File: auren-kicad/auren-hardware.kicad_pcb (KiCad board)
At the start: 2 copper layers, 24 x 18 mm, 11 parts, among them J1 USB_B_Mini, J2 USB_B_Mini, J3 Speaker_1, J4 Speaker_2, J5 Speaker_1, J6 Speaker_2

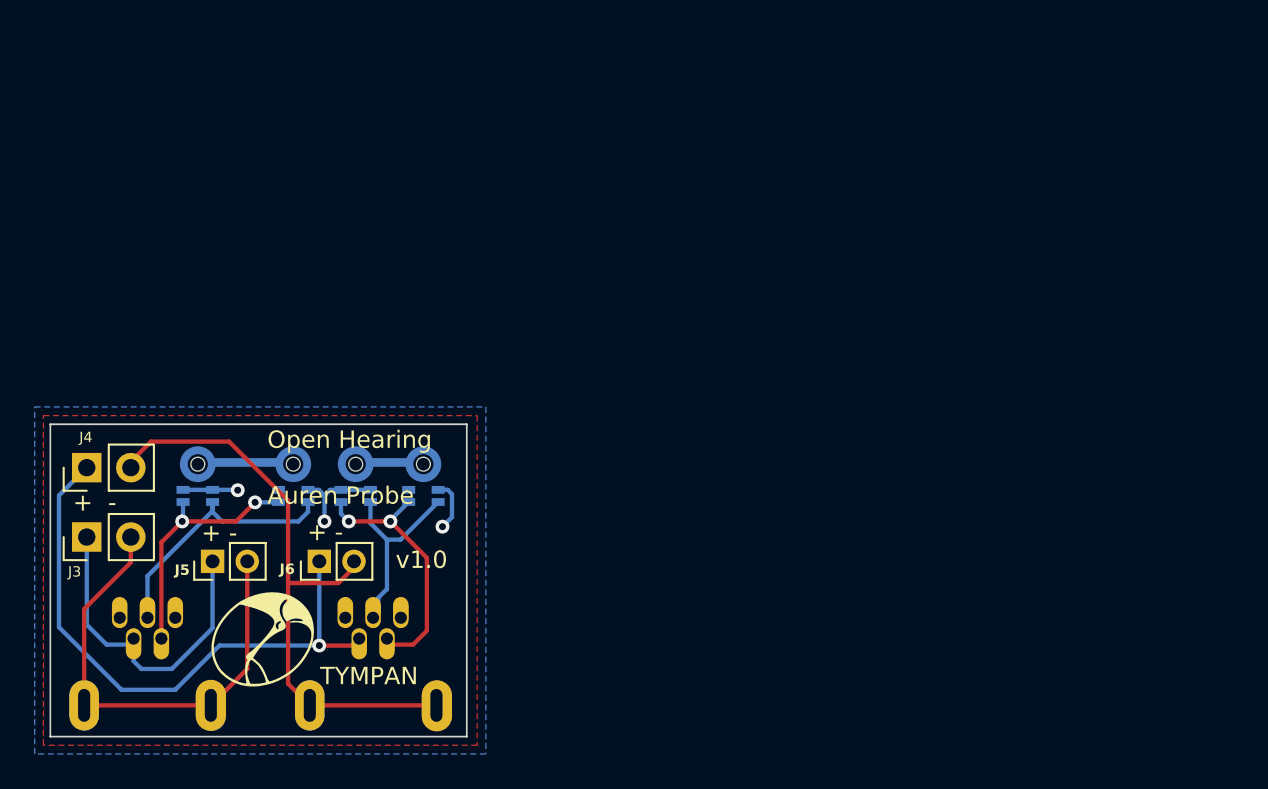
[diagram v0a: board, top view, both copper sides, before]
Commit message: Added outline shape files
Imported DXF to PCB layout file and converted to board outline.
Rough component placement
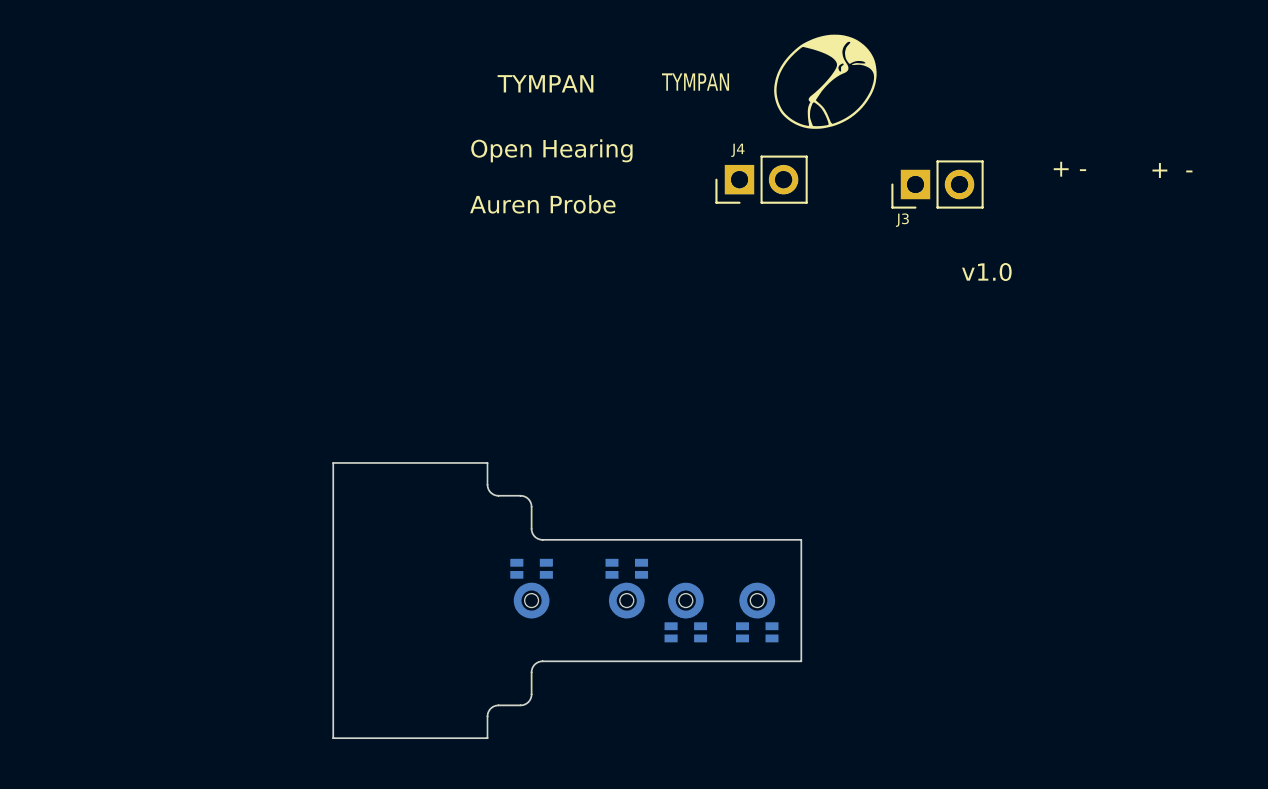
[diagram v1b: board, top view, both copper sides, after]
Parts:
- removed J1, J2: USB_B_Mini, Flywheel:MOLEX_56579-0519
- removed J5: Speaker_1, Connector_PinHeader_2.00mm:PinHeader_1x02_P2.00mm_Vertical
- removed J6: Speaker_2, Connector_PinHeader_2.00mm:PinHeader_1x02_P2.00mm_Vertical
- moved J3 51.9 mm to (169.4, 81.2)
- moved G*** 45.7 mm to (164.2, 75.3)
- moved J4 41.1 mm to (159.2, 80.9)
- moved MIC4 20.8 mm to (160.2, 105.2)
- moved MIC1 20.8 mm to (147.2, 105.2), turned to -90 degrees
- moved MIC2 20.8 mm to (152.7, 105.2), turned to -90 degrees
- moved MIC3 20.6 mm to (156.1, 105.2)
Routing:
- net /SPK2-: track 35.4 -> 0.00 mm
- net /SPK2+: track 34.7 -> 0.00 mm, vias 1 -> 0
- net /SPK1-: track 27.9 -> 0.00 mm
- net /SPK1+: track 19.2 -> 0.00 mm
- net /DAT_1: track 15.3 -> 0.00 mm
- net /CLK_2: track 15.2 -> 0.00 mm, vias 2 -> 0
- net /CLK_1: track 14.4 -> 0.00 mm, vias 2 -> 0
- net VDD: track 11.5 -> 0.00 mm, vias 3 -> 0
- net /DAT_2: track 11.2 -> 0.00 mm
- net GND: track 10.6 -> 0.00 mm
- removed copper zone on B.Cu, net GND
- removed copper zone on F.Cu, net VDD
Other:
- board size 24 x 18 mm -> 27 x 15.9 mm
- board text added: "1"
- board text added: "2"
- board text added: "3"
- board text added: "4"
- board text added: "A"
- board text added: "B"
- board text added: "C"
- board text added: "D"
- board text added: "MIC ports are 0.8mm diameter"

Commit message: minor edit
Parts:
- moved J3 32.3 mm to (142.5, 99.1), turned to 0 degrees
- moved J4 28.2 mm to (137.7, 99.1), turned to 0 degrees
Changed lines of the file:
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@@
 	(footprint "Connector_PinHeader_2.54mm:PinHeader_1x02_P2.54mm_Vertical"
 		(layer "F.Cu")
-		(at 169.3586 81.1824 90)
+		(at 142.46 99.1098)
 		(descr "Through hole straight pin header, 1x02, 2.54mm pitch, single row")
 		(tags "Through hole pin header THT 1x02 2.54mm single row")
 		(property "Reference" "J3"
-			(at -2 -0.7 0)
+			(at -0.127 4.5516 180)
 			(layer "F.SilkS")
 			(effects
@@
 		)
 		(property "Value" "Speaker_1"
-			(at 0 4.87 270)
+			(at 0 4.87 0)
 			(layer "F.Fab")
 			(effects
@@
 		)
 		(property "Datasheet" ""
-			(at 0 0 90)
+			(at 0 0 0)
 			(unlocked yes)
 			(layer "F.Fab")
@@
 		)
 		(property "Description" ""
-			(at 0 0 90)
+			(at 0 0 0)
 			(unlocked yes)
 			(layer "F.Fab")
@@
 		)
 		(fp_line
-			(start 1.33 1.27)
-			(end 1.33 3.87)
-			(stroke
-				(width 0.12)
-				(type solid)
-			)
-			(layer "F.SilkS")
-		)
-		(fp_line
-			(start -1.33 1.27)
-			(end 1.33 1.27)
-			(stroke
-				(width 0.12)
-				(type solid)
-			)
-			(layer "F.SilkS")
-		)
-		(fp_line
-			(start -1.33 1.27)
+			(start -1.33 1.270001)
 			(end -1.33 3.87)
+			(stroke
+				(width 0.12)
+				(type solid)
+			)
+			(layer "F.SilkS")
+		)
+		(fp_line
+			(start -1.33 1.270001)
+			(end 1.33 1.270001)
 			(stroke
 				(width 0.12)
@@
 		)
 		(fp_line
+			(start 1.33 1.270001)
+			(end 1.33 3.87)
+			(stroke
+				(width 0.12)
+				(type solid)
+			)
+			(layer "F.SilkS")
+		)
+		(fp_line
+			(start -1.8 -1.8)
+			(end -1.8 4.35)
+			(stroke
+				(width 0.05)
+				(type solid)
+			)
+			(layer "F.CrtYd")
+		)
+		(fp_line
+			(start -1.8 4.35)
+			(end 1.8 4.35)
+			(stroke
+				(width 0.05)
+				(type solid)
+			)
+			(layer "F.CrtYd")
+		)
+		(fp_line
 			(start 1.8 -1.8)
 			(end -1.8 -1.8)
@@
 		)
 		(fp_line
-			(start -1.8 -1.8)
-			(end -1.8 4.35)
-			(stroke
-				(width 0.05)
-				(type solid)
-			)
-			(layer "F.CrtYd")
-		)
-		(fp_line
 			(start 1.8 4.35)
 			(end 1.8 -1.8)
@@
 		)
 		(fp_line
-			(start -1.8 4.35)
-			(end 1.8 4.35)
-			(stroke
-				(width 0.05)
-				(type solid)
-			)
-			(layer "F.CrtYd")
+			(start -1.27 -0.635)
+			(end -0.635 -1.27)
+			(stroke
+				(width 0.1)
+				(type solid)
+			)
+			(layer "F.Fab")
+		)
+		(fp_line
+			(start -1.27 3.81)
+			(end -1.27 -0.635)
+			(stroke
+				(width 0.1)
+				(type solid)
+			)
+			(layer "F.Fab")
+		)
+		(fp_line
+			(start -0.635 -1.27)
+			(end 1.27 -1.27)
+			(stroke
+				(width 0.1)
+				(type solid)
+			)
+			(layer "F.Fab")
 		)
 		(fp_line
@@
 		)
 		(fp_line
-			(start -0.635 -1.27)
-			(end 1.27 -1.27)
-			(stroke
-				(width 0.1)
-				(type solid)
-			)
-			(layer "F.Fab")
-		)
-		(fp_line
-			(start -1.27 -0.635)
-			(end -0.635 -1.27)
-			(stroke
-				(width 0.1)
-				(type solid)
-			)
-			(layer "F.Fab")
-		)
-		(fp_line
 			(start 1.27 3.81)
 			(end -1.27 3.81)
@@
 			(layer "F.Fab")
 		)
-		(fp_line
-			(start -1.27 3.81)
-			(end -1.27 -0.635)
-			(stroke
-				(width 0.1)
-				(type solid)
-			)
-			(layer "F.Fab")
-		)
 		(fp_text user "${REFERENCE}"
-			(at 0 1.27 0)
+			(at 0 1.270001 90)
 			(layer "F.Fab")
 			(effects
@@
 		)
 		(pad "1" thru_hole rect
-			(at 0 0 90)
+			(at 0 0)
 			(size 1.7 1.7)
 			(drill 1)
@@
 		)
 		(pad "2" thru_hole oval
-			(at 0 2.54 90)
+			(at 0 2.54)
 			(size 1.7 1.7)
 			(drill 1)
@@
 	(footprint "Connector_PinHeader_2.54mm:PinHeader_1x02_P2.54mm_Vertical"
 		(layer "F.Cu")
-		(at 159.219 80.903 90)
+		(at 137.7102 99.1098)
 		(descr "Through hole straight pin header, 1x02, 2.54mm pitch, single row")
 		(tags "Through hole pin header THT 1x02 2.54mm single row")
 		(property "Reference" "J4"
-			(at 1.75 -0.05 0)
+			(at -0.0762 4.5262 180)
 			(layer "F.SilkS")
 			(effects
@@
 		)
 		(property "Value" "Speaker_2"
-			(at 0 4.87 270)
+			(at 0 4.87 0)
 			(layer "F.Fab")
 			(effects
@@
 		)
 		(property "Datasheet" ""
-			(at 0 0 90)
+			(at 0 0 0)
 			(unlocked yes)
 			(layer "F.Fab")
@@
 		)
 		(property "Description" ""
-			(at 0 0 90)
+			(at 0 0 0)
 			(unlocked yes)
 			(layer "F.Fab")
@@
 		)
 		(fp_line
-			(start 1.33 1.27)
-			(end 1.33 3.87)
-			(stroke
-				(width 0.12)
-				(type solid)
-			)
-			(layer "F.SilkS")
-		)
-		(fp_line
-			(start -1.33 1.27)
-			(end 1.33 1.27)
-			(stroke
-				(width 0.12)
-				(type solid)
-			)
-			(layer "F.SilkS")
-		)
-		(fp_line
-			(start -1.33 1.27)
+			(start -1.33 1.270001)
 			(end -1.33 3.87)
+			(stroke
+				(width 0.12)
+				(type solid)
+			)
+			(layer "F.SilkS")
+		)
+		(fp_line
+			(start -1.33 1.270001)
+			(end 1.33 1.270001)
 			(stroke
 				(width 0.12)
@@
 		)
 		(fp_line
+			(start 1.33 1.270001)
+			(end 1.33 3.87)
+			(stroke
+				(width 0.12)
+				(type solid)
+			)
+			(layer "F.SilkS")
+		)
+		(fp_line
+			(start -1.8 -1.8)
+			(end -1.8 4.35)
+			(stroke
+				(width 0.05)
+				(type solid)
+			)
+			(layer "F.CrtYd")
+		)
+		(fp_line
+			(start -1.8 4.35)
+			(end 1.8 4.35)
+			(stroke
+				(width 0.05)
+				(type solid)
+			)
+			(layer "F.CrtYd")
+		)
+		(fp_line
 			(start 1.8 -1.8)
 			(end -1.8 -1.8)
@@
 		)
 		(fp_line
-			(start -1.8 -1.8)
-			(end -1.8 4.35)
-			(stroke
-				(width 0.05)
-				(type solid)
-			)
-			(layer "F.CrtYd")
-		)
-		(fp_line
 			(start 1.8 4.35)
 			(end 1.8 -1.8)
@@
 		)
 		(fp_line
-			(start -1.8 4.35)
-			(end 1.8 4.35)
-			(stroke
-				(width 0.05)
-				(type solid)
-			)
-			(layer "F.CrtYd")
+			(start -1.27 -0.635)
+			(end -0.635 -1.27)
+			(stroke
+				(width 0.1)
+				(type solid)
+			)
+			(layer "F.Fab")
+		)
+		(fp_line
+			(start -1.27 3.81)
+			(end -1.27 -0.635)
+			(stroke
+				(width 0.1)
+				(type solid)
+			)
+			(layer "F.Fab")
+		)
+		(fp_line
+			(start -0.635 -1.27)
+			(end 1.27 -1.27)
+			(stroke
+				(width 0.1)
+				(type solid)
+			)
+			(layer "F.Fab")
 		)
 		(fp_line
@@
 		)
 		(fp_line
-			(start -0.635 -1.27)
-			(end 1.27 -1.27)
-			(stroke
-				(width 0.1)
-				(type solid)
-			)
-			(layer "F.Fab")
-		)
-		(fp_line
-			(start -1.27 -0.635)
-			(end -0.635 -1.27)
-			(stroke
-				(width 0.1)
-				(type solid)
-			)
-			(layer "F.Fab")
-		)
-		(fp_line
 			(start 1.27 3.81)
 			(end -1.27 3.81)
@@
 			(layer "F.Fab")
 		)
-		(fp_line
-			(start -1.27 3.81)
-			(end -1.27 -0.635)
-			(stroke
-				(width 0.1)
-				(type solid)
-			)
-			(layer "F.Fab")
-		)
 		(fp_text user "${REFERENCE}"
-			(at 0 1.27 0)
+			(at 0 1.270001 90)
 			(layer "F.Fab")
 			(effects
@@
 		)
 		(pad "1" thru_hole rect
-			(at 0 0 90)
+			(at 0 0)
 			(size 1.7 1.7)
 			(drill 1)
@@
 		)
 		(pad "2" thru_hole oval
-			(at 0 2.54 90)
+			(at 0 2.54)
 			(size 1.7 1.7)
 			(drill 1)

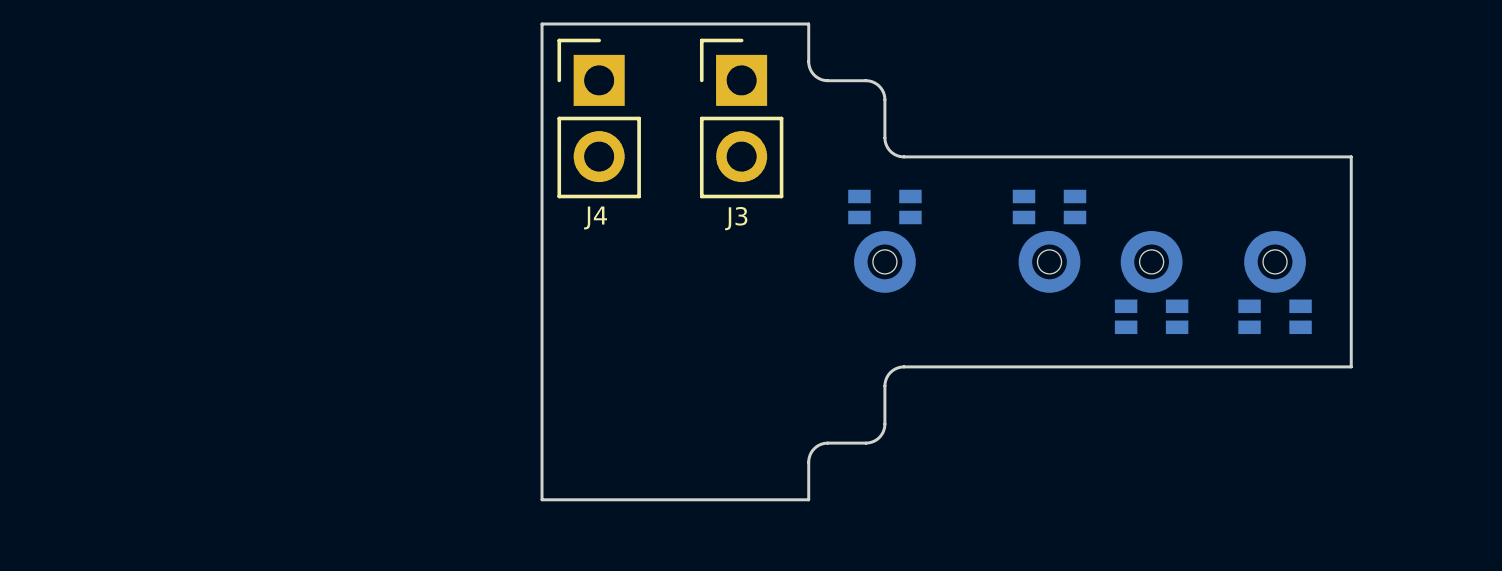
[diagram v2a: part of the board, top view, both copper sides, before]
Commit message: Added microHDMI datasheets
Imported first draft PCB outline
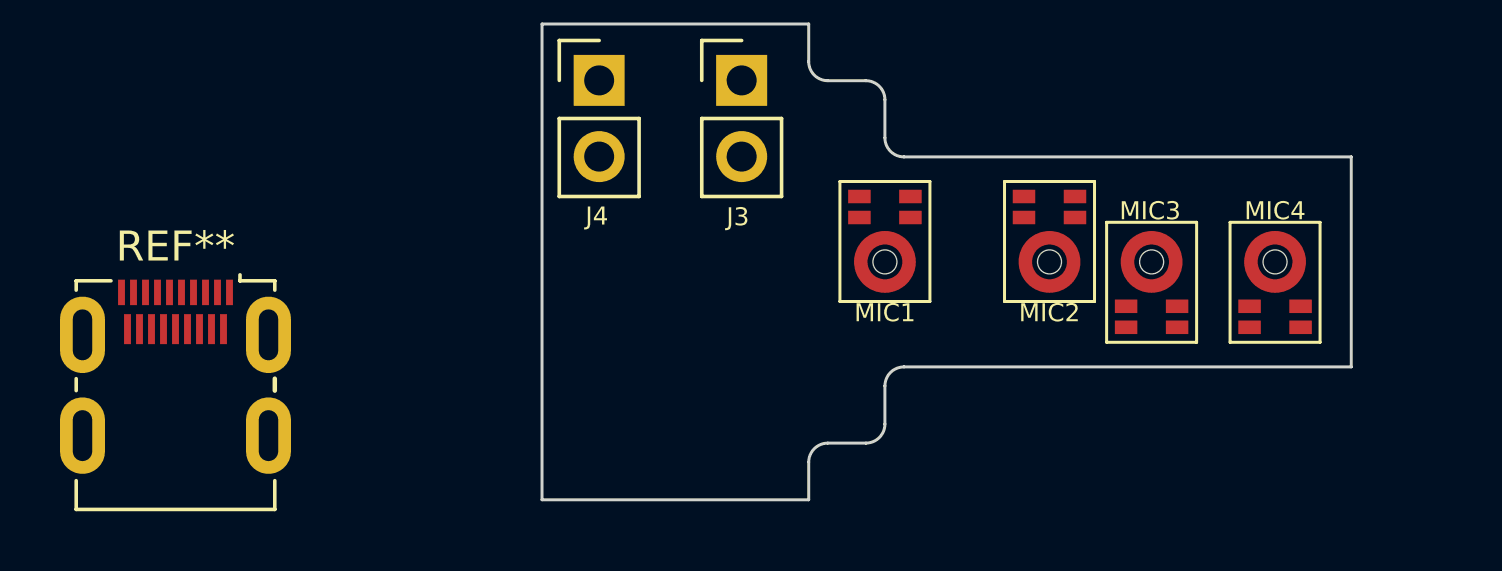
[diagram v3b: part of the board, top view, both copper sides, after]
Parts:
- added REF**: HDMI_Micro-D_Molex_46765-1x01, Connector_Video:HDMI_Micro-D_Molex_46765-1x01, F.Cu at (123.6, 111.0)
- MIC1, MIC2, MIC3, MIC4: moved to F.Cu
